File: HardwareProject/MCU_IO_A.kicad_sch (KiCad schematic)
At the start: 11 parts, among them U23 TPD4E05U06DQA, U4 HPM6P41IPB1

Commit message: 换其他电感之前暂存一下
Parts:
- removed R25, R26, R27, R28: 100Ω, Resistor_SMD:R_0603_1608Metric, symbol 02_HPM_Resistor:100Ω_0402
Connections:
- net PA4 is gone; now on net J_TDO: U23.1 (D1+), U23.10 (NC), U4.15 (PA04/UART1.CTS/SPI1.SCLK/MCAN0.RXD/PWM0.P4/TRGM.P04/QEI0.H0/SEI0.CK/JTAG.TDO)
- net PA5 is gone; now on net J_TDI: U23.4 (D2+), U23.7 (NC), U4.14 (PA05/GPTMR1.COMP2/UART1.DE/UART1.RTS/SPI1.CS0/MCAN0.TXD/PWM0.P5/TRGM.P05/ETH0.RXCK/QEI0.Z/QEO0.Z/SEI0.DE/JTAG.TDI)
- net PA6 is gone; now on net J_TCK: U23.2 (D1-), U23.9 (NC), U4.13 (PA06/GPTMR0.CAPT0/UART1.RXD/SPI1.MISO/PWM0.P6/TRGM.P06/ETH0.RXDV/QEI0.B/QEO0.B/SEI0.RX/JTAG.TCK)
- net PA7 is gone; now on net J_TMS: U23.5 (D2-), U23.6 (NC), U4.12 (PA07/GPTMR0.COMP0/UART1.TXD/SPI1.MOSI/PWM0.P7/TRGM.P07/ETH0.RXER/QEI0.A/QEO0.A/SEI0.TX/JTAG.TMS)

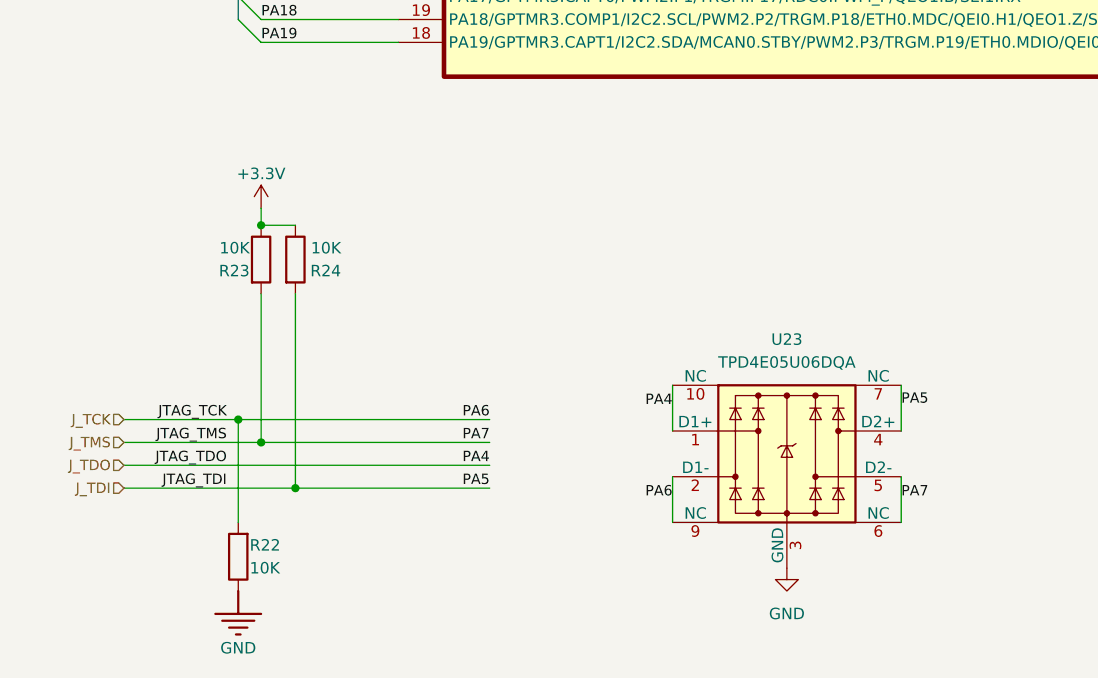
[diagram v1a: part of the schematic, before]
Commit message: 完成Rev4 电源 驱动 模拟 IO
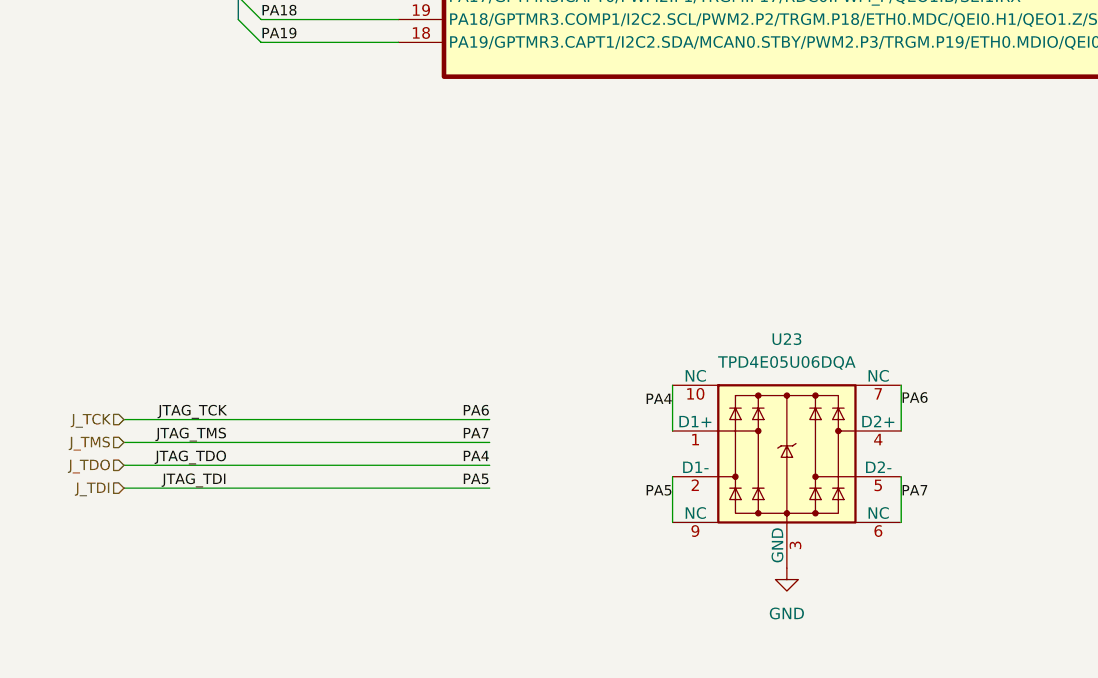
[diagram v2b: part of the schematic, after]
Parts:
- removed R22, R23, R24: 10K, Resistor_SMD:R_0603_1608Metric, symbol 02_HPM_Resistor:10K_0402
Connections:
- net J_TCK: now also U23.4 (D2+), U23.7 (NC); no longer U23.2 (D1-), U23.9 (NC)
- net J_TDI: now also U23.2 (D1-), U23.9 (NC); no longer U23.4 (D2+), U23.7 (NC)

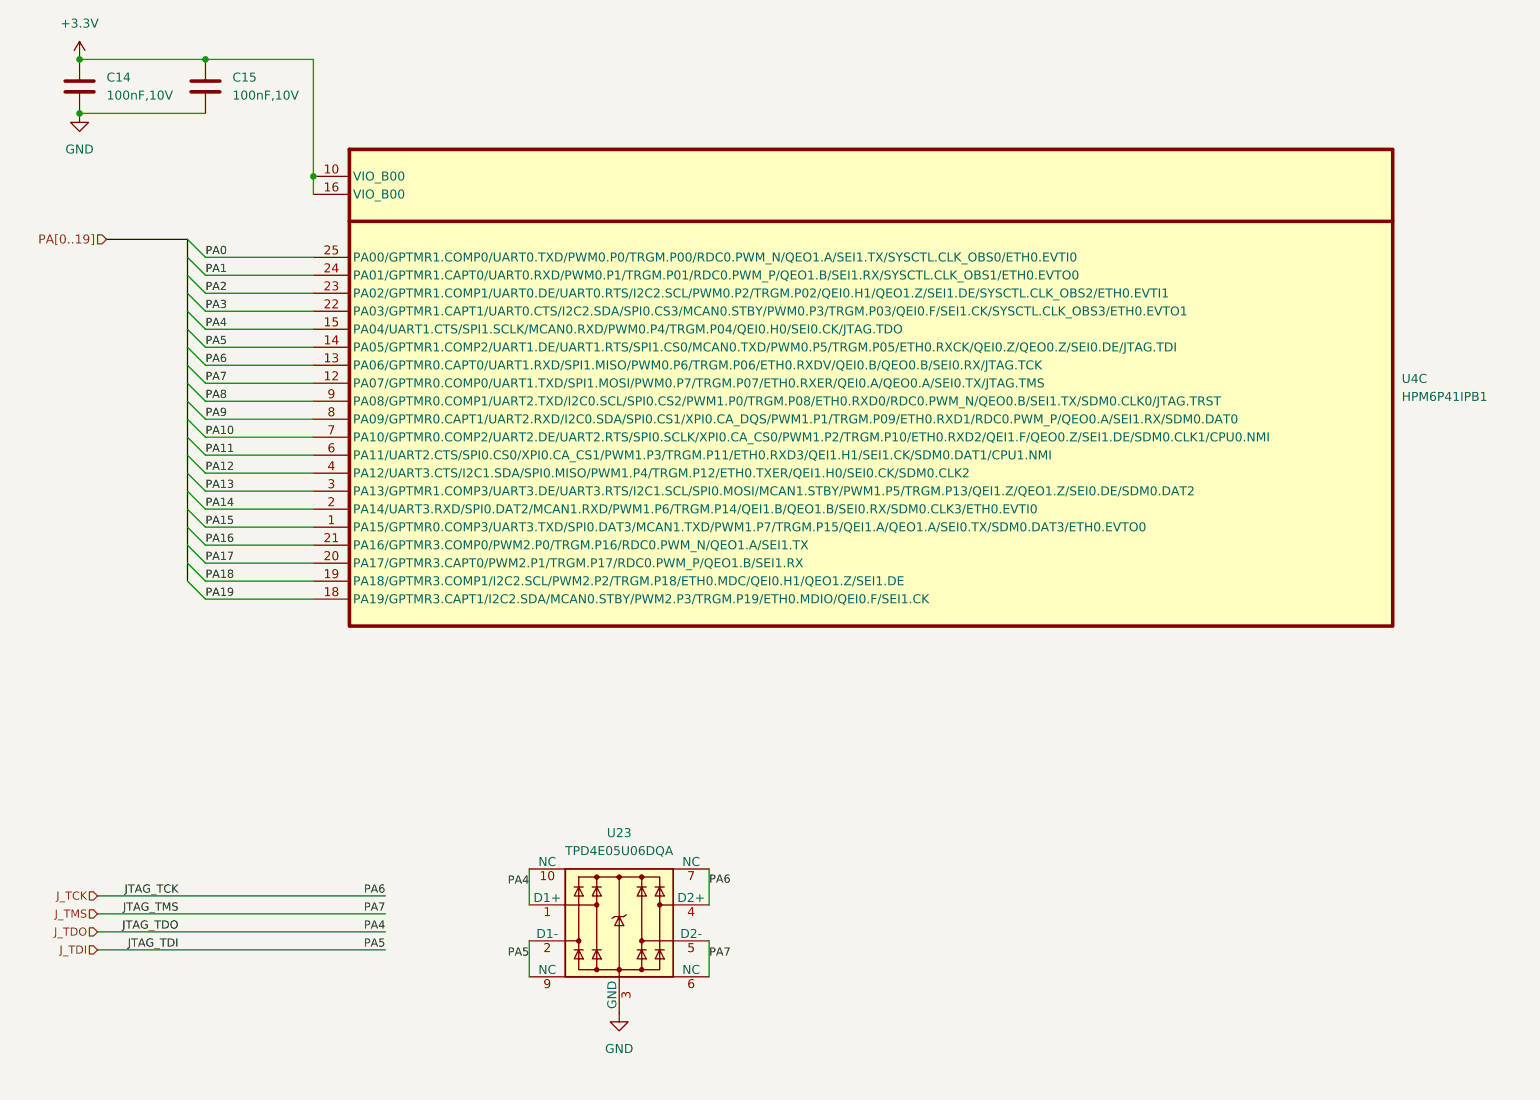
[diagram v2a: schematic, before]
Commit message: rev4修改核心供电前保存（当前SYR838）
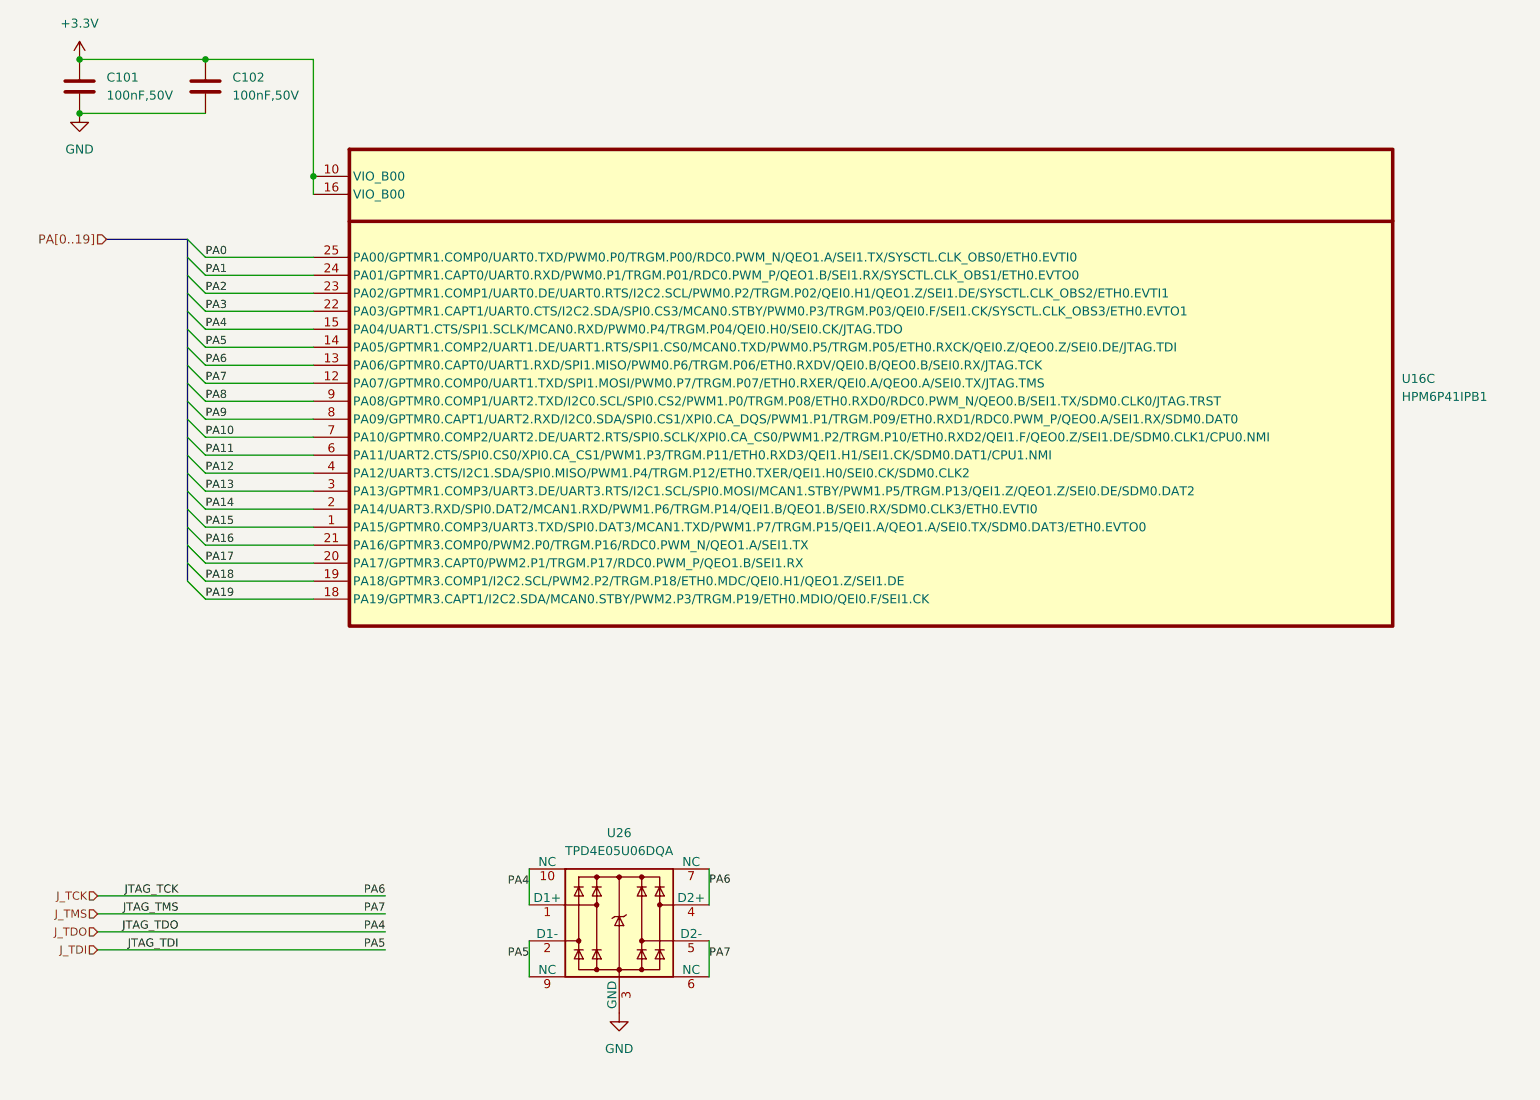
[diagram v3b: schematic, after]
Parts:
- C101: renamed from C14; value 100nF,10V -> 100nF,50V
- C102: renamed from C15; value 100nF,10V -> 100nF,50V
- renumbered U4 to U16, U23 to U26
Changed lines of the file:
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@@
 		(on_board yes)
 		(dnp no)
-		(property "Reference" "C14"
+		(property "Reference" "C101"
 			(at 57.15 46.9899 0)
 			(effects
@@
 			)
 		)
-		(property "Value" "100nF,10V"
+		(property "Value" "100nF,50V"
 			(at 57.15 49.5299 0)
 			(effects
@@
 			(project "HPM6P41_BB"
 				(path "/714b8a30-f9a7-49d4-a000-bc20c4884c7a/10595600-bc6b-49c1-b1d2-c8f5864aa8f2"
-					(reference "C14")
+					(reference "C101")
 					(unit 1)
 				)
@@
 		(dnp no)
 		(fields_autoplaced yes)
-		(property "Reference" "#PWR030"
+		(property "Reference" "#PWR0192"
 			(at 53.34 58.42 0)
 			(effects
@@
 			(project "HPM6P41_BB"
 				(path "/714b8a30-f9a7-49d4-a000-bc20c4884c7a/10595600-bc6b-49c1-b1d2-c8f5864aa8f2"
-					(reference "#PWR030")
+					(reference "#PWR0192")
 					(unit 1)
 				)
@@
 		(on_board yes)
 		(dnp no)
-		(property "Reference" "C15"
+		(property "Reference" "C102"
 			(at 74.93 46.9899 0)
 			(effects
@@
 			)
 		)
-		(property "Value" "100nF,10V"
+		(property "Value" "100nF,50V"
 			(at 74.93 49.5299 0)
 			(effects
@@
 			(project "HPM6P41_BB"
 				(path "/714b8a30-f9a7-49d4-a000-bc20c4884c7a/10595600-bc6b-49c1-b1d2-c8f5864aa8f2"
-					(reference "C15")
+					(reference "C102")
 					(unit 1)
 				)
@@
 		(dnp no)
 		(fields_autoplaced yes)
-		(property "Reference" "#PWR0180"
+		(property "Reference" "#PWR0193"
 			(at 129.54 185.42 0)
 			(effects
@@
 			(project "HPM6P41_BB"
 				(path "/714b8a30-f9a7-49d4-a000-bc20c4884c7a/10595600-bc6b-49c1-b1d2-c8f5864aa8f2"
-					(reference "#PWR0180")
+					(reference "#PWR0193")
 					(unit 1)
 				)
@@
 		(dnp no)
 		(fields_autoplaced yes)
-		(property "Reference" "U4"
+		(property "Reference" "U16"
 			(at 240.03 89.5349 0)
 			(effects
@@
 			(project "HPM6P41_BB"
 				(path "/714b8a30-f9a7-49d4-a000-bc20c4884c7a/10595600-bc6b-49c1-b1d2-c8f5864aa8f2"
-					(reference "U4")
+					(reference "U16")
 					(unit 3)
 				)
@@
 		(dnp no)
 		(fields_autoplaced yes)
-		(property "Reference" "#PWR029"
+		(property "Reference" "#PWR0191"
 			(at 53.34 48.26 0)
 			(effects
@@
 			(project "HPM6P41_BB"
 				(path "/714b8a30-f9a7-49d4-a000-bc20c4884c7a/10595600-bc6b-49c1-b1d2-c8f5864aa8f2"
-					(reference "#PWR029")
+					(reference "#PWR0191")
 					(unit 1)
 				)
@@
 		(on_board yes)
 		(dnp no)
-		(property "Reference" "U23"
+		(property "Reference" "U26"
 			(at 129.54 153.67 0)
 			(effects
@@
 			(project "HPM6P41_BB"
 				(path "/714b8a30-f9a7-49d4-a000-bc20c4884c7a/10595600-bc6b-49c1-b1d2-c8f5864aa8f2"
-					(reference "U23")
+					(reference "U26")
 					(unit 1)
 				)
